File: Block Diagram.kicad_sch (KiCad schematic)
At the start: 0 parts

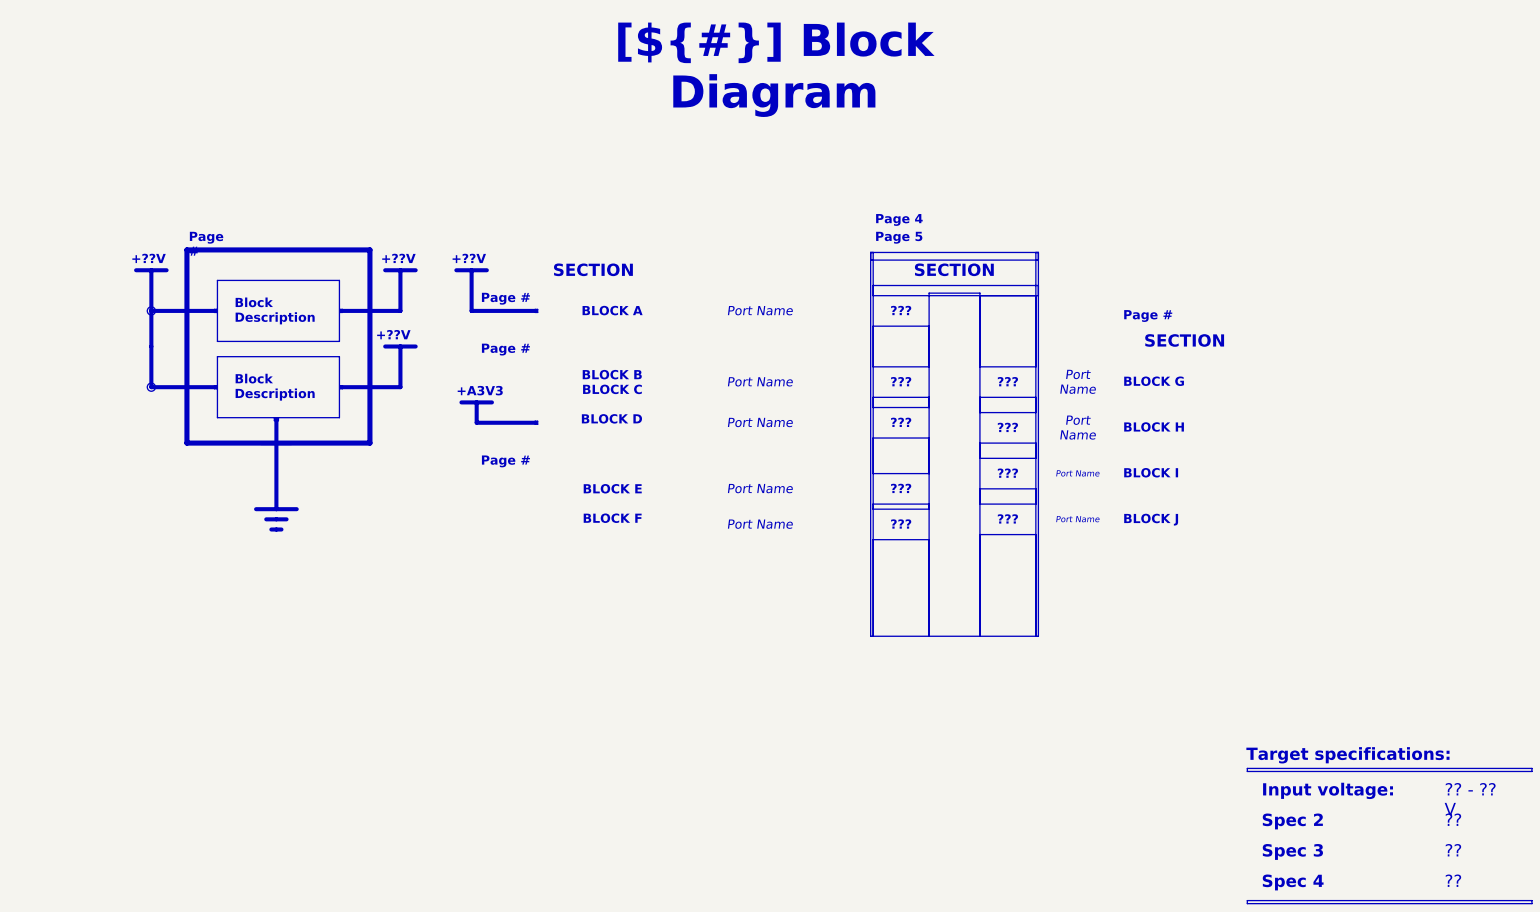
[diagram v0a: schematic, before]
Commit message: SCH[Inital Setup]: Created intital pages, added some inital symbols.
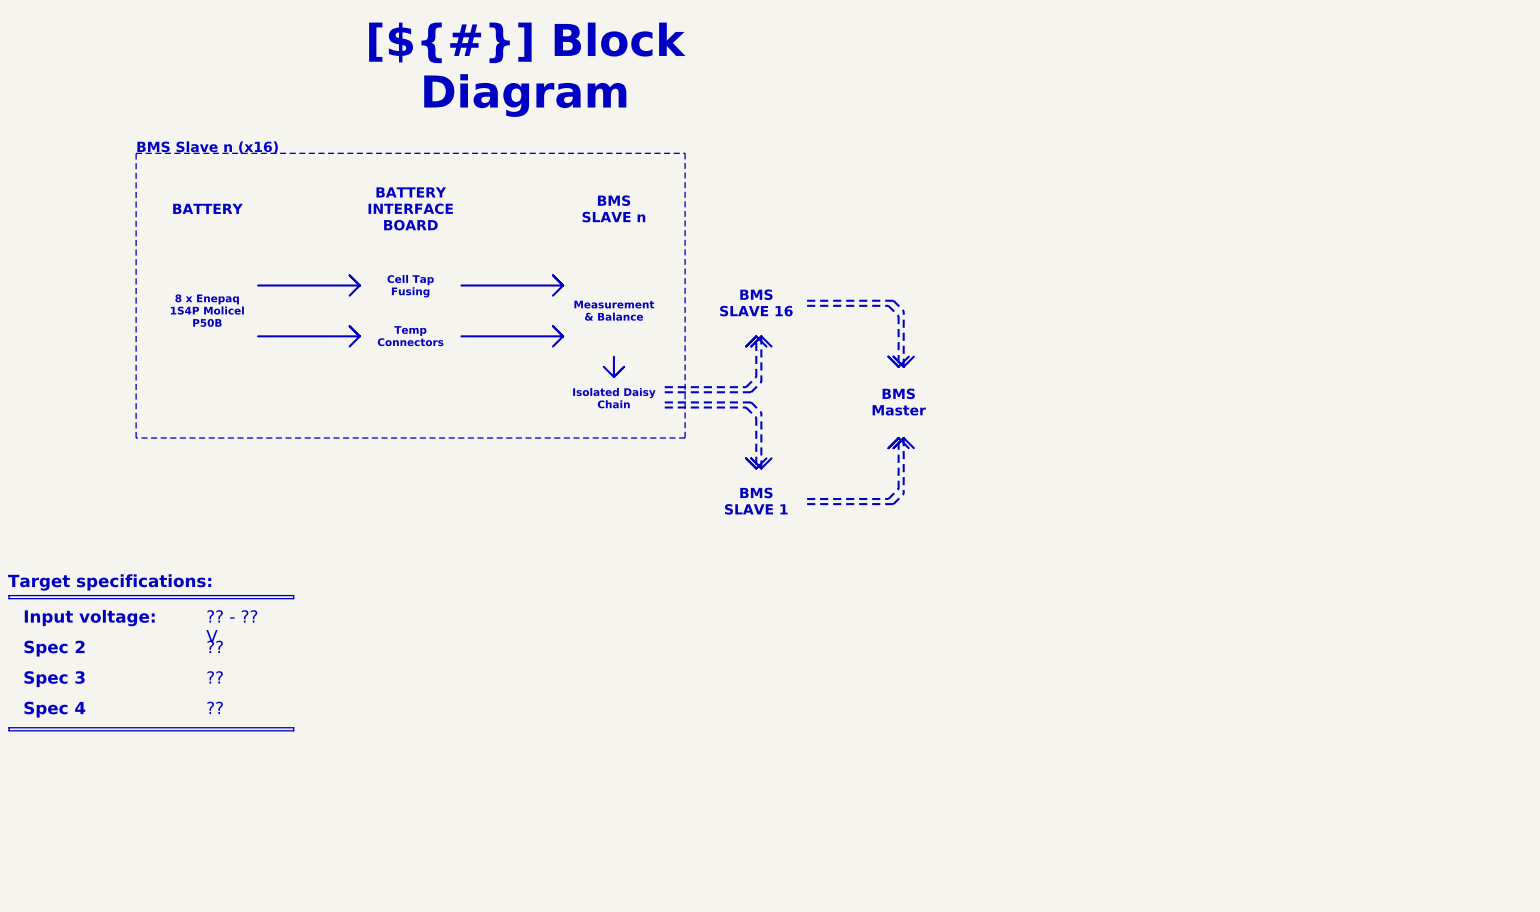
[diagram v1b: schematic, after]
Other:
- note added: "BMS Slave n (x16)"
- note removed: "+??V"
- note removed: "+A3V3"
